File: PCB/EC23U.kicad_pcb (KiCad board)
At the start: 2 copper layers, 77.1 x 137.6 mm, 85 parts, among them J1 JST, J2 RGB, SW1 BOOT0, SW10 EC_SW, SW11 EC_SW, SW12 EC_SW, SW13 EC_SW, SW14 EC_SW, SW15 EC_SW, SW16 EC_SW, SW17 EC_SW, SW18 EC_SW, SW19 EC_SW, SW2 EC_SW, SW20 EC_SW, SW21 EC_SW, SW22 EC_SW, SW23 EC_SW, SW24 EC_SW, SW25 EC_SW, SW26 EC_SW, SW27 EC_SW, SW28 EC_SW, SW3 EC_SW, SW4 EC_SW, SW5 EC_SW, SW6 EC_SW, SW7 EC_SW, SW8 EC_SW, SW9 EC_SW, U1 STM32F401CBUx, U2 XC6206PxxxMR, U3 74HC4051, U4 OPA350, U5 SN74AHCT1G125, Y1 8 MHz

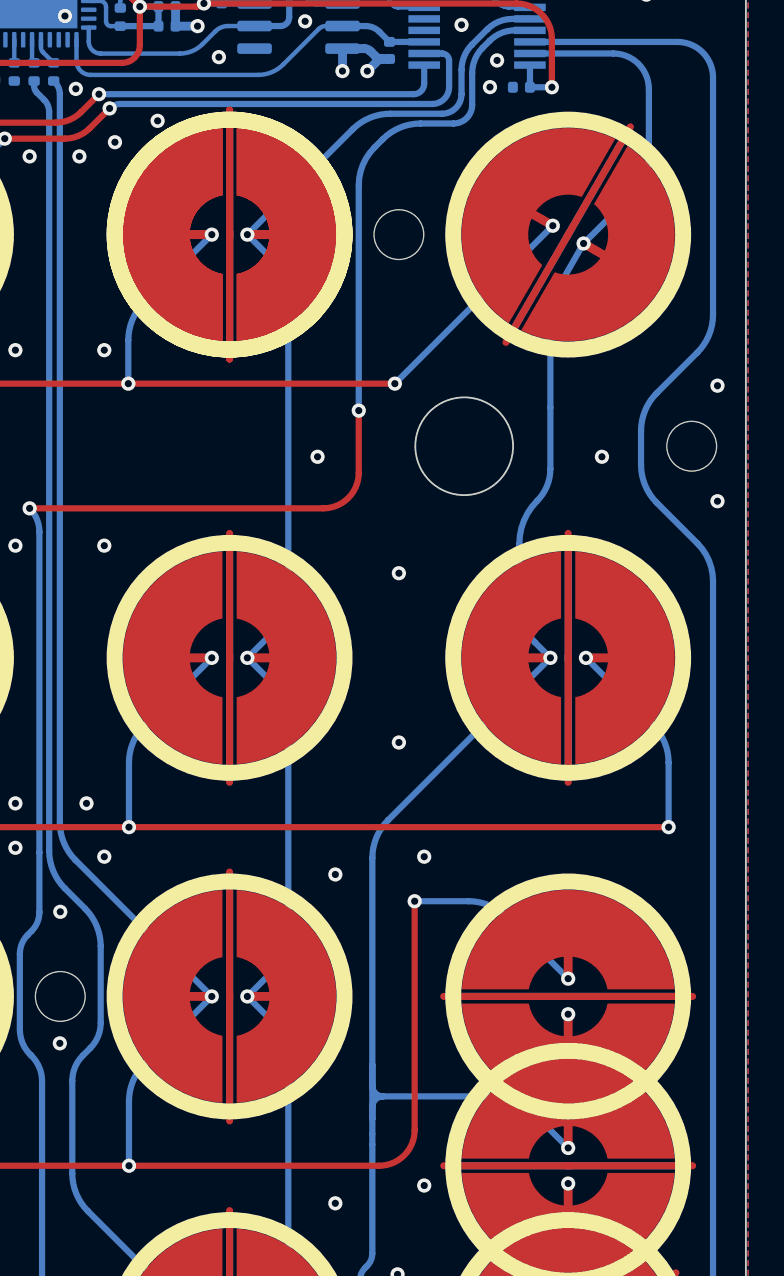
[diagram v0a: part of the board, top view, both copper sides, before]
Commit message: Update for 3d models
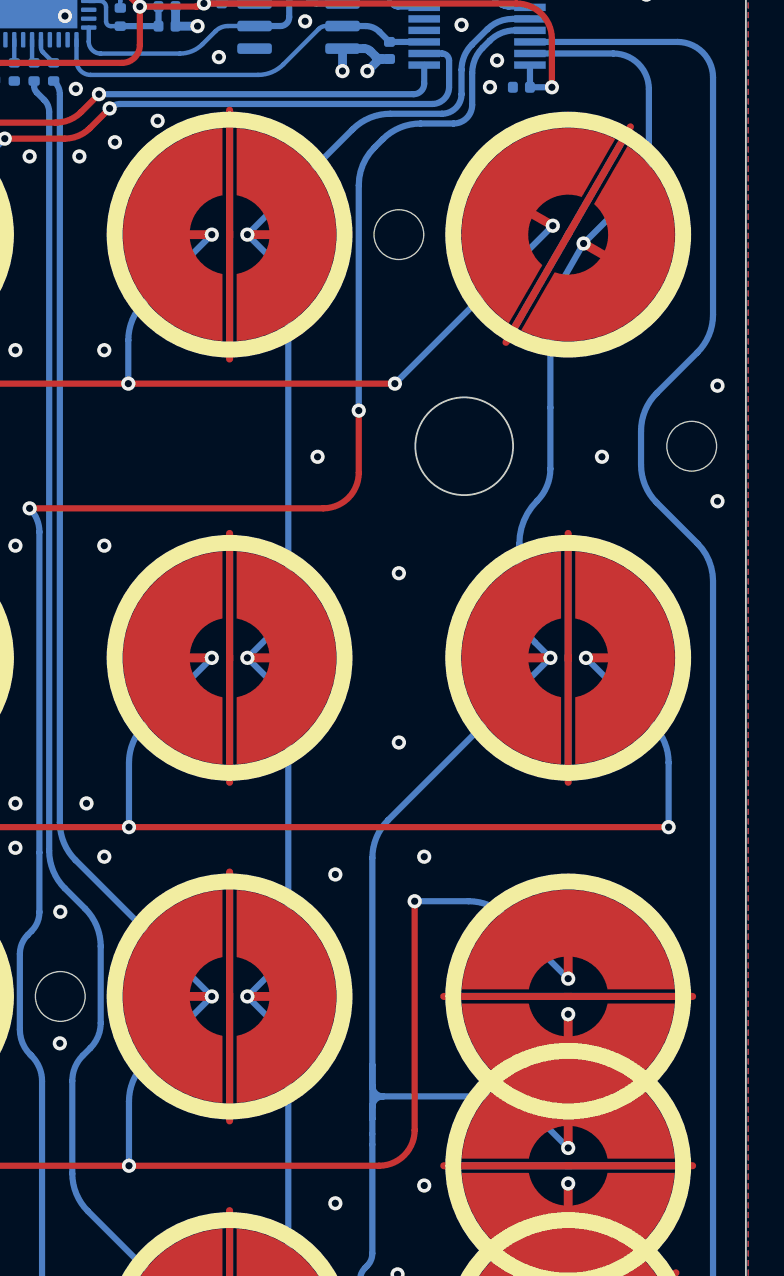
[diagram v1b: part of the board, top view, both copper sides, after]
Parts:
- removed the SW4 at (137.2, 49.0)
- SW10, SW11, SW12, SW13, SW15, SW16, SW17, SW18, SW19, SW2, SW20, SW21, SW22, SW24, SW25, SW26, SW27, SW3, SW4, SW5, SW6, SW7, SW8, SW9: footprint cipulot_parts:ecs_pad_no_ring -> cipulot_parts:ecs_pad_1U_no_ring
- SW14, SW23, SW28: footprint cipulot_parts:ecs_pad_no_ring -> cipulot_parts:ecs_pad_2U_no_ring
- turned SW14 to 90 degrees
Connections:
- SW14 pad 1: SENSE_3 -> STROBE_3
- SW14 pad 2: STROBE_3 -> SENSE_3
